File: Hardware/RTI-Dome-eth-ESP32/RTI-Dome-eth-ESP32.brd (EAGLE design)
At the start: 111.1 x 76.3 mm, 99 parts, among them IC2 24LC64T-I/SN, IC8 REG1117-3.3V, J1 691313510003, J10 691313510002, J11 691313510002, J12 691313510002, J2 XT60PW-M, J3 691313510003, J4 691313510003, J6 691313510003, J7 691313510003, J8 691313510002, J9 691313510002, T1 MMBT3904LT1, T2 MMBT3904LT1, T3 MMBT3904LT1, U1 W5500, U2 ESP32-DevKitC-32UE, X9 J1011F01PNL

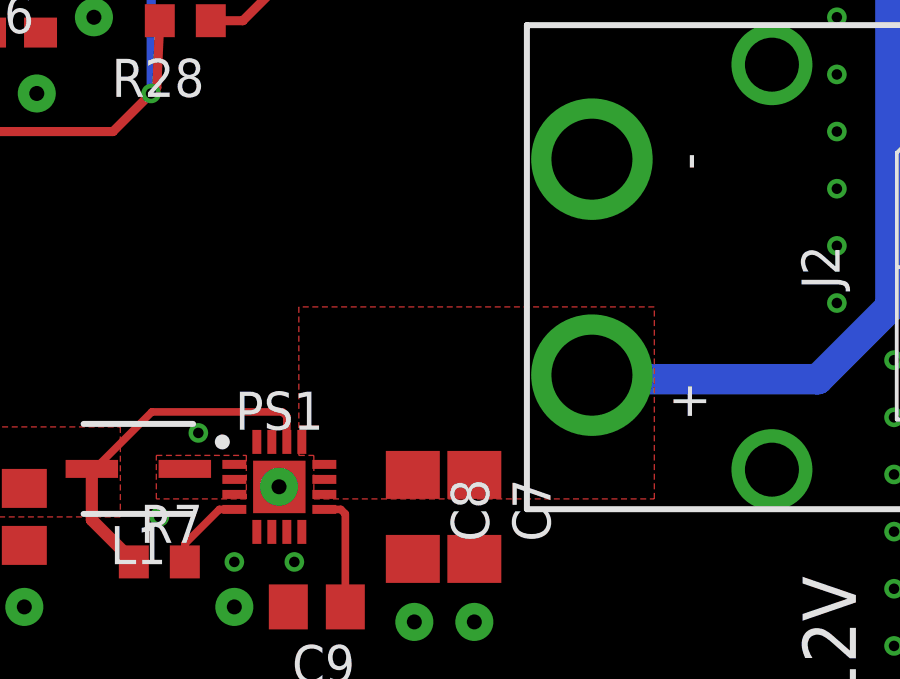
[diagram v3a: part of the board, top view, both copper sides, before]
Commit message: Better 12V input filtering
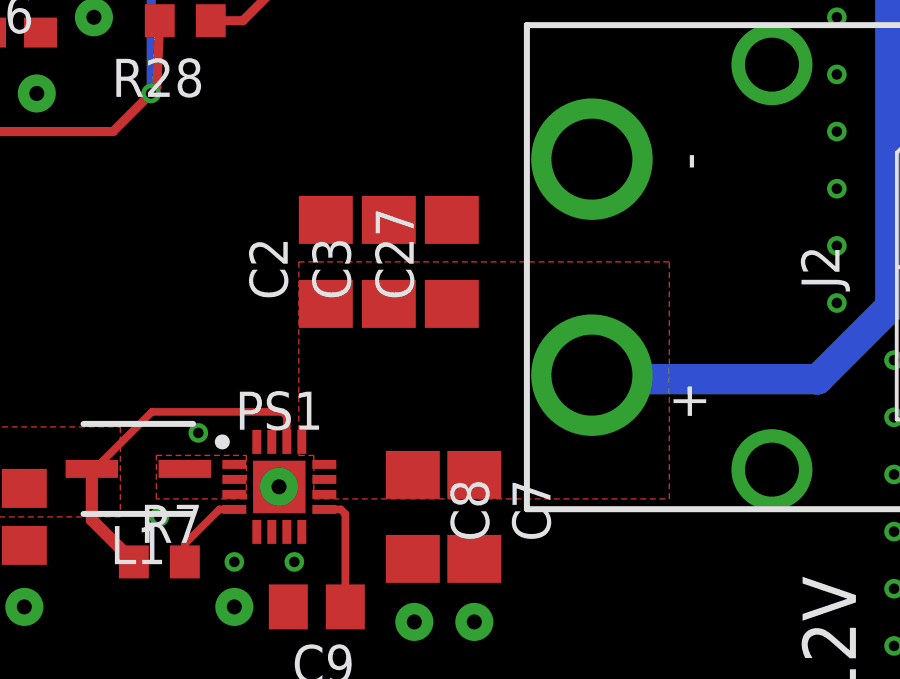
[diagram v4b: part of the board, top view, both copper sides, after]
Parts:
- added C2, C27, C3: 22uF 35V, rcl:C1206
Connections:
- net +12V: now also C2.1, C27.1, C3.1
- net GND: now also C2.2, C27.2, C3.2
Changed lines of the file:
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@@
 <attribute name="VALUE" x="84.04" y="15.73" size="1.27" layer="27" rot="R90"/>
+</element>
+<element name="C2" library="rcl" library_urn="urn:adsk.eagle:library:334" package="C1206" package3d_urn="urn:adsk.eagle:package:23618/2" value="22uF 35V" x="91.55" y="25.5" smashed="yes" rot="R90">
+<attribute name="NAME" x="90.28" y="24.23" size="1.27" layer="25" rot="R90"/>
+<attribute name="POPULARITY" value="54" x="91.55" y="25.5" size="1.778" layer="27" rot="R90" display="off"/>
+<attribute name="SPICEPREFIX" value="C" x="91.55" y="25.5" size="1.778" layer="27" rot="R90" display="off"/>
+<attribute name="VALUE" x="94.09" y="24.23" size="1.27" layer="27" rot="R90"/>
+</element>
+<element name="C3" library="rcl" library_urn="urn:adsk.eagle:library:334" package="C1206" package3d_urn="urn:adsk.eagle:package:23618/2" value="22uF 35V" x="93.65" y="25.5" smashed="yes" rot="R90">
+<attribute name="NAME" x="92.38" y="24.23" size="1.27" layer="25" rot="R90"/>
+<attribute name="POPULARITY" value="54" x="93.65" y="25.5" size="1.778" layer="27" rot="R90" display="off"/>
+<attribute name="SPICEPREFIX" value="C" x="93.65" y="25.5" size="1.778" layer="27" rot="R90" display="off"/>
+<attribute name="VALUE" x="96.19" y="24.23" size="1.27" layer="27" rot="R90"/>
+</element>
+<element name="C27" library="rcl" library_urn="urn:adsk.eagle:library:334" package="C1206" package3d_urn="urn:adsk.eagle:package:23618/2" value="22uF 35V" x="95.75" y="25.5" smashed="yes" rot="R90">
+<attribute name="NAME" x="94.48" y="24.23" size="1.27" layer="25" rot="R90"/>
+<attribute name="POPULARITY" value="54" x="95.75" y="25.5" size="1.778" layer="27" rot="R90" display="off"/>
+<attribute name="SPICEPREFIX" value="C" x="95.75" y="25.5" size="1.778" layer="27" rot="R90" display="off"/>
+<attribute name="VALUE" x="98.29" y="24.23" size="1.27" layer="27" rot="R90"/>
 </element>
 </elements>
@@
 <via x="86" y="17" extent="1-16" drill="0.35"/>
 <via x="90.5" y="15.5" extent="1-16" drill="0.35"/>
+<contactref element="C2" pad="2"/>
+<contactref element="C27" pad="2"/>
+<contactref element="C3" pad="2"/>
 </signal>
 <signal name="+12V" class="1">
@@
 <polygon width="0.1016" layer="1" thermals="no">
 <vertex x="91.15" y="17.6"/>
-<vertex x="102.5" y="17.6"/>
-<vertex x="102.5" y="24"/>
-<vertex x="90.65" y="24"/>
+<vertex x="103" y="17.6"/>
+<vertex x="103" y="25.5"/>
+<vertex x="90.65" y="25.5"/>
 <vertex x="90.65" y="19.05"/>
 <vertex x="91.15" y="19.05"/>
 </polygon>
+<contactref element="C2" pad="1"/>
+<contactref element="C27" pad="1"/>
+<contactref element="C3" pad="1"/>
 </signal>
 <signal name="SHUTTER_OPENED">

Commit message: Re-export board from Fusion
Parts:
- JP1: value (none) -> 3PIN_Header
- moved U2 0.75 mm to (26.6, 47.0)
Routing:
- net ETH_CS: track 57.1 -> 58.0 mm
- net HOME_SHUTTER_CLOSED: track 32.2 -> 32.9 mm
- net M_STEP: track 66.2 -> 66.8 mm
- net SPARE1_IN_5V: track 40.9 -> 41.5 mm
- net SPARE2_IN_5V: track 30.9 -> 30.4 mm
